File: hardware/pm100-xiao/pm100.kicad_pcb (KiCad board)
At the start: 2 copper layers, 39.1 x 68.6 mm, 42 parts, among them J1 VCC-BATT, J10 NRST, J2 VCC-ESC, J4 GND-BATT, J5 UART, J6 RECEIVER, J7 ESC, J8 SWDIO, J9 SWCLK, Q5 BSS138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

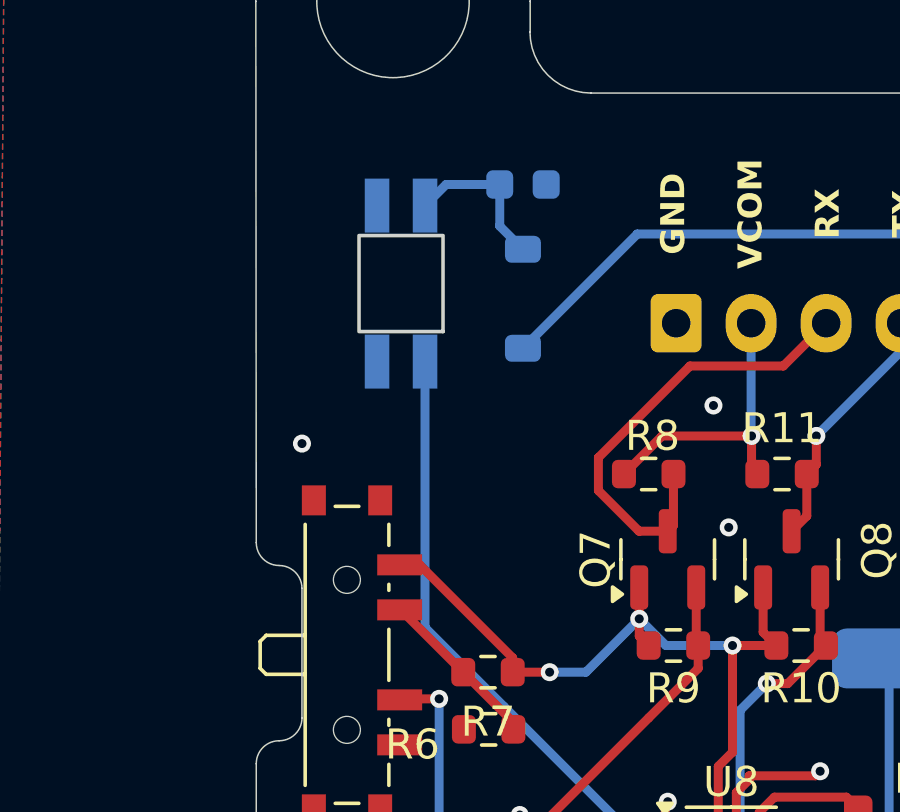
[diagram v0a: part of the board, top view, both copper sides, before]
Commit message: ajustando pinagem LED RGBA
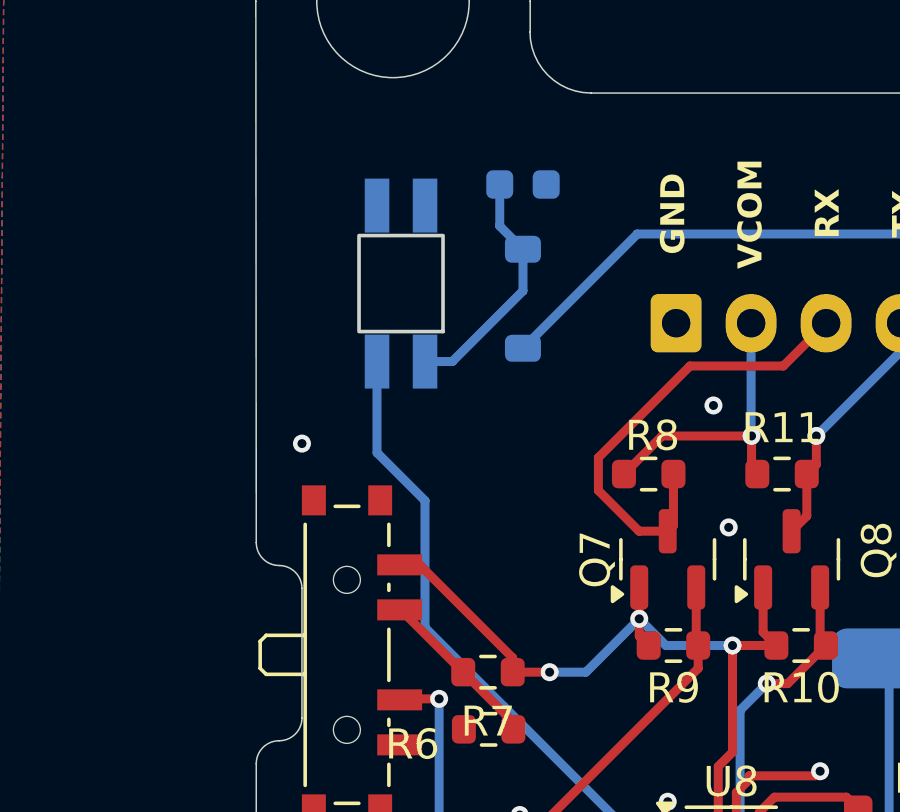
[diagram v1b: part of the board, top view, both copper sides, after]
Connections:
- D2 pad 1: Net-(D2-VDD) -> unconnected-(D2-DOUT-Pad1)
- D2 pad 2: unconnected-(D2-DOUT-Pad2) -> GND
- D2 pad 3: GND -> LED
- D2 pad 4: LED -> Net-(D2-VDD)
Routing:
- net Net-(D2-VDD): track 5.26 -> 8.11 mm
- net LED: track 42.9 -> 43.5 mm
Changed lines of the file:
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@@
 	(net 11 "PWM-ESC")
 	(net 12 "PWM-OUTPUT")
-	(net 13 "unconnected-(D2-DOUT-Pad2)")
+	(net 13 "unconnected-(D2-DOUT-Pad1)")
 	(net 14 "Net-(U8-Vin+)")
 	(net 15 "Net-(U8-Vin-)")
@@
 			(size 1.8 0.82)
 			(layers "B.Cu" "B.Mask" "B.Paste")
-			(net 25 "Net-(D2-VDD)")
-			(pinfunction "VDD")
-			(pintype "power_in")
+			(net 13 "unconnected-(D2-DOUT-Pad1)")
+			(pinfunction "DOUT")
+			(pintype "output")
 			(thermal_bridge_angle 45)
 		)
@@
 			(size 1.8 0.82)
 			(layers "B.Cu" "B.Mask" "B.Paste")
-			(net 13 "unconnected-(D2-DOUT-Pad2)")
-			(pinfunction "DOUT")
-			(pintype "output")
+			(net 1 "GND")
+			(pinfunction "VSS")
+			(pintype "power_in")
 			(thermal_bridge_angle 45)
 		)
@@
 			(size 1.8 0.82)
 			(layers "B.Cu" "B.Mask" "B.Paste")
-			(net 1 "GND")
-			(pinfunction "VSS")
-			(pintype "power_in")
+			(net 26 "LED")
+			(pinfunction "DIN")
+			(pintype "input")
 			(thermal_bridge_angle 45)
 		)
@@
 			(size 1.8 0.82)
 			(layers "B.Cu" "B.Mask" "B.Paste")
-			(net 26 "LED")
-			(pinfunction "DIN")
-			(pintype "input")
+			(net 25 "Net-(D2-VDD)")
+			(pinfunction "VDD")
+			(pintype "power_in")
 			(thermal_bridge_angle 45)
 		)
 		(embedded_fonts no)
-		(model "${SIGMA}/LED_SK6812MINI-E.step"
+		(model "${KIPRJMOD}/3d/LED_SK6812MINI-E.step"
 			(offset
 				(xyz 0 5.08 -1.75)
@@
 	)
 	(segment
-		(start 139.932 44.958)
-		(end 139.23 45.66)
+		(start 139.23 50.86)
+		(end 140.14 50.86)
 		(width 0.3)
 		(layer "B.Cu")
@@
 	)
 	(segment
-		(start 141.719 44.958)
-		(end 139.932 44.958)
+		(start 140.14 50.86)
+		(end 142.494 48.506)
+		(width 0.3)
+		(layer "B.Cu")
+		(net 25)
+	)
+	(segment
+		(start 142.494 48.506)
+		(end 142.494 47.118)
 		(width 0.3)
 		(layer "B.Cu")
@@
 	)
 	(segment
-		(start 139.23 50.86)
-		(end 139.23 59.728)
+		(start 139.23 55.5)
+		(end 137.63 53.9)
+		(width 0.3)
+		(layer "B.Cu")
+		(net 26)
+	)
+	(segment
+		(start 137.63 53.9)
+		(end 137.63 50.86)
 		(width 0.3)
 		(layer "B.Cu")
@@
 		(width 0.3)
 		(layer "B.Cu")
+		(net 26)
+	)
+	(segment
+		(start 139.23 55.5)
+		(end 139.23 59.728)
+		(width 0.3)
+		(layer "B.Cu")
